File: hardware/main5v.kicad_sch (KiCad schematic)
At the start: 4 parts, among them U701 TPS56837RPAR

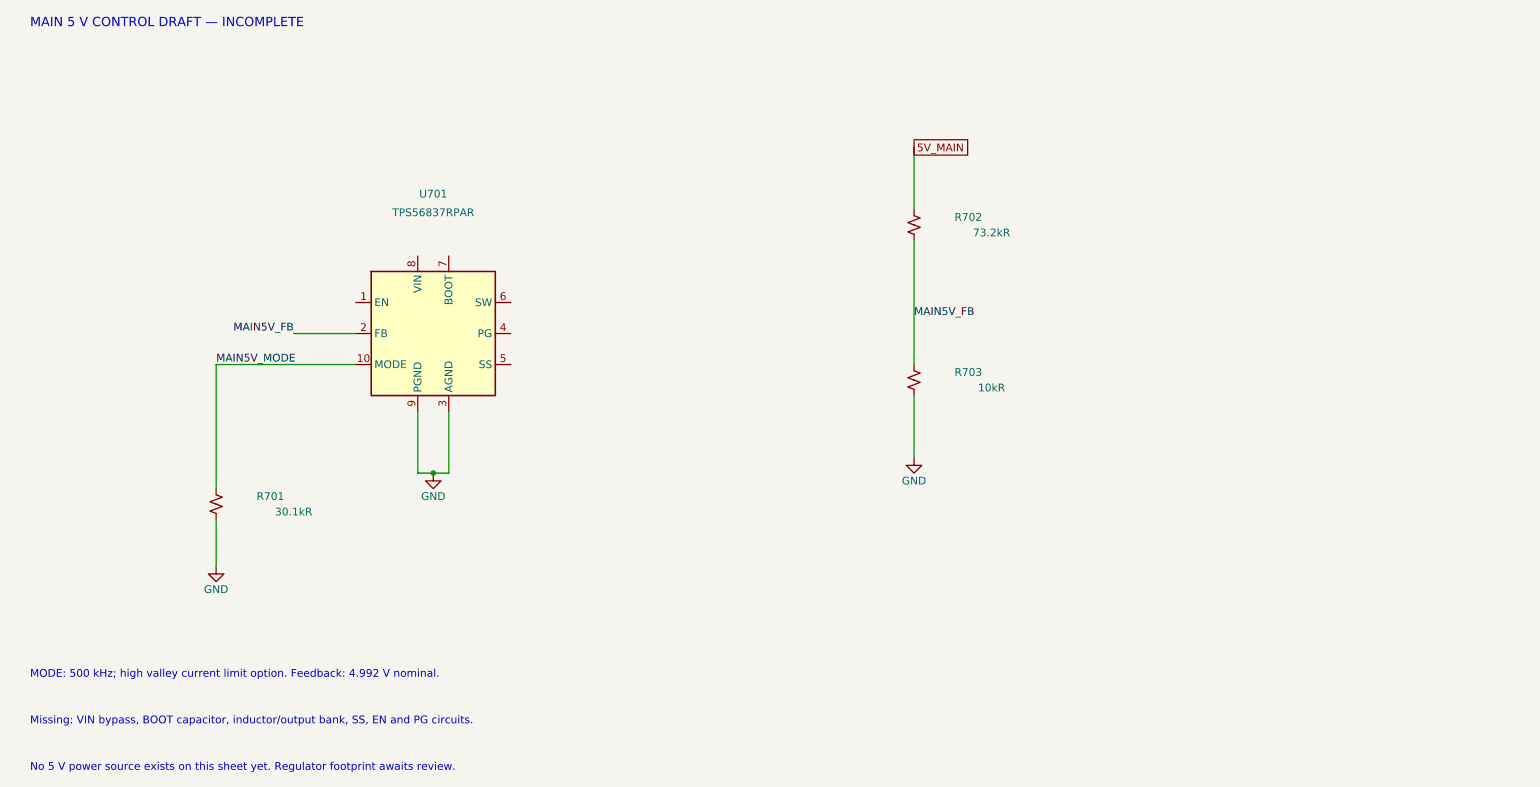
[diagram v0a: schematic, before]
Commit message: Capture main 5 V bootstrap capacitor with native connectivity checks
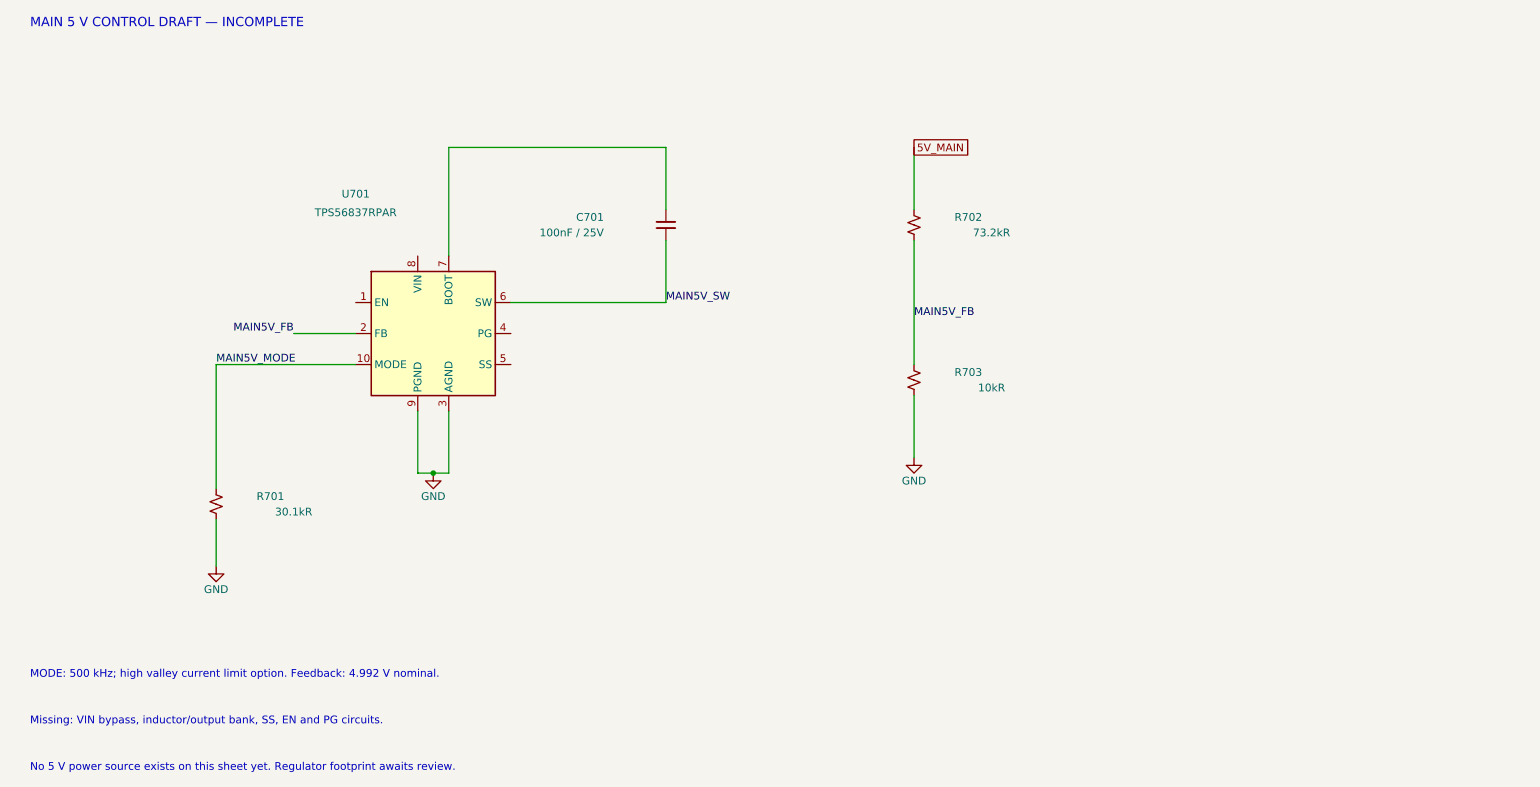
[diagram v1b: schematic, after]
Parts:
- added C701: 100nF / 25V, Capacitor_SMD:C_0603_1608Metric, symbol Device:C_Small
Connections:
- net MAIN5V_SW: now reaches U701.6 (SW)
- net MAIN5V_SW: now also C701.2
- net at U701.7 (BOOT): now also C701.1
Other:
- note added: "Missing: VIN bypass, inductor/output bank, SS, EN and PG circuits."
- note removed: "Missing: VIN bypass, BOOT capacitor, inductor/output bank, SS, EN and PG circuits."

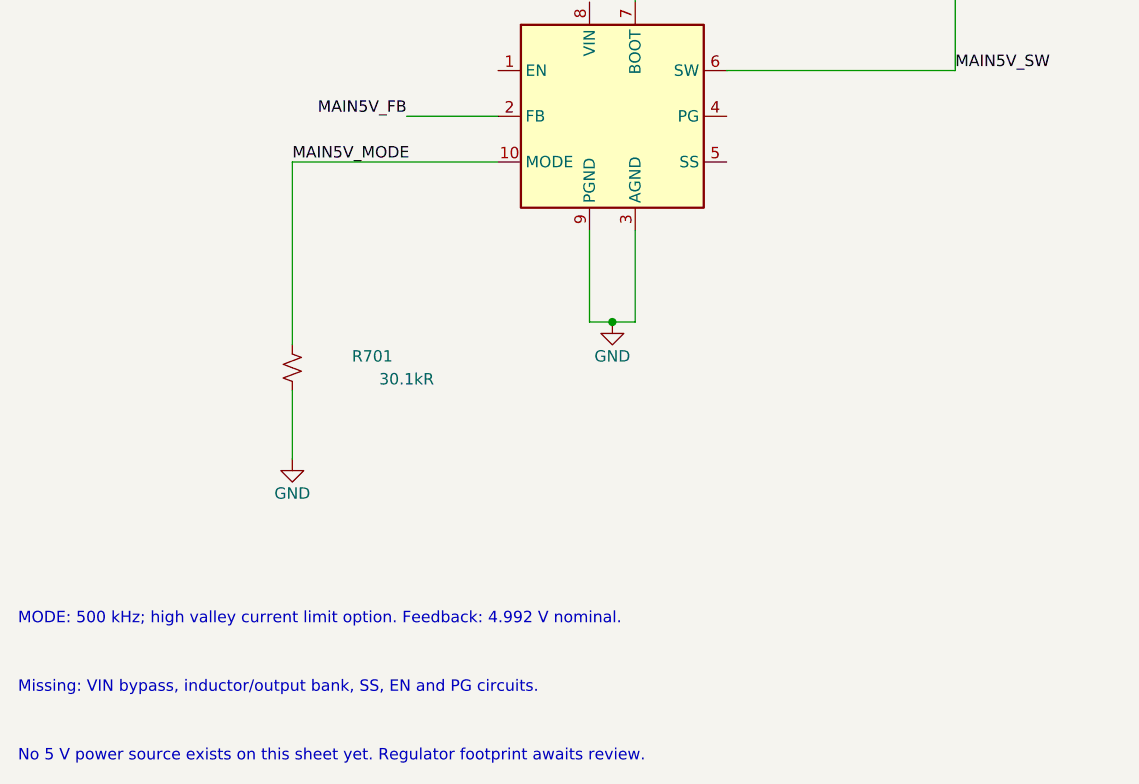
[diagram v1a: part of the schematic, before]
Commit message: Capture main 5 V soft start with exact manufacturer capacitor
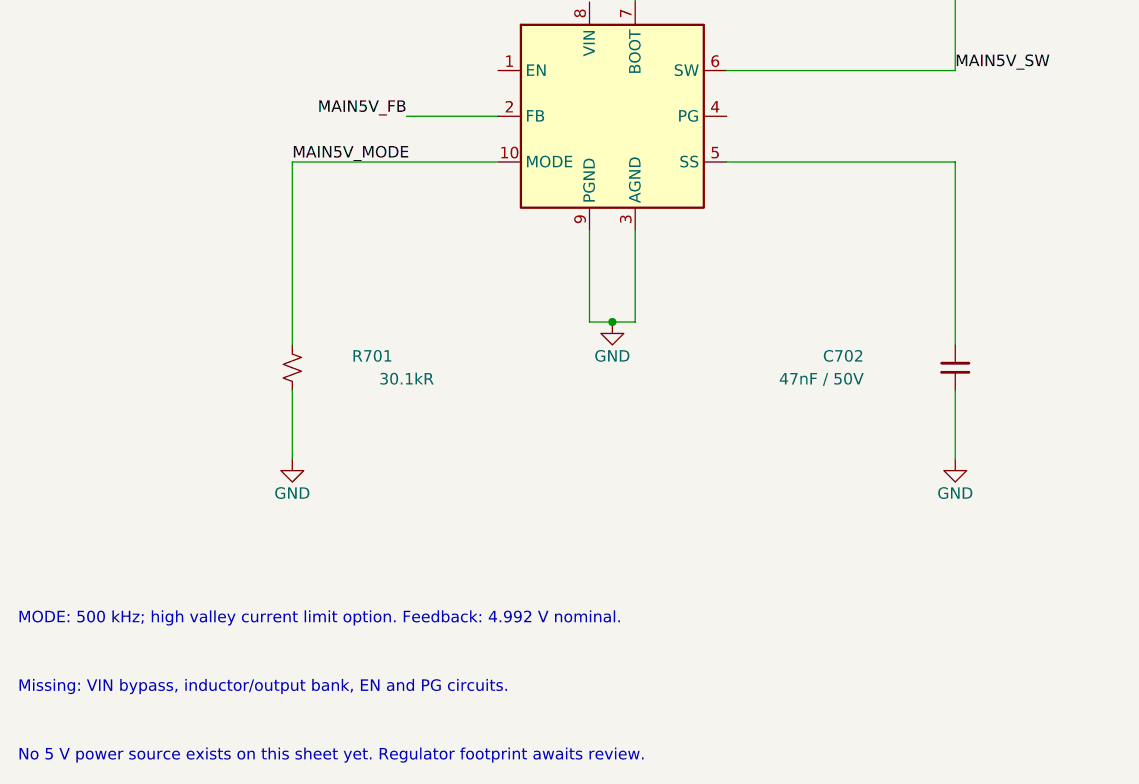
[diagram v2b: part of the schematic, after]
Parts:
- added C702: 47nF / 50V, Capacitor_SMD:C_0603_1608Metric, symbol Device:C_Small
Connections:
- net GND: now also C702.2
- net at U701.5 (SS): now also C702.1
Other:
- note added: "Missing: VIN bypass, inductor/output bank, EN and PG circuits."
- note removed: "Missing: VIN bypass, inductor/output bank, SS, EN and PG circuits."

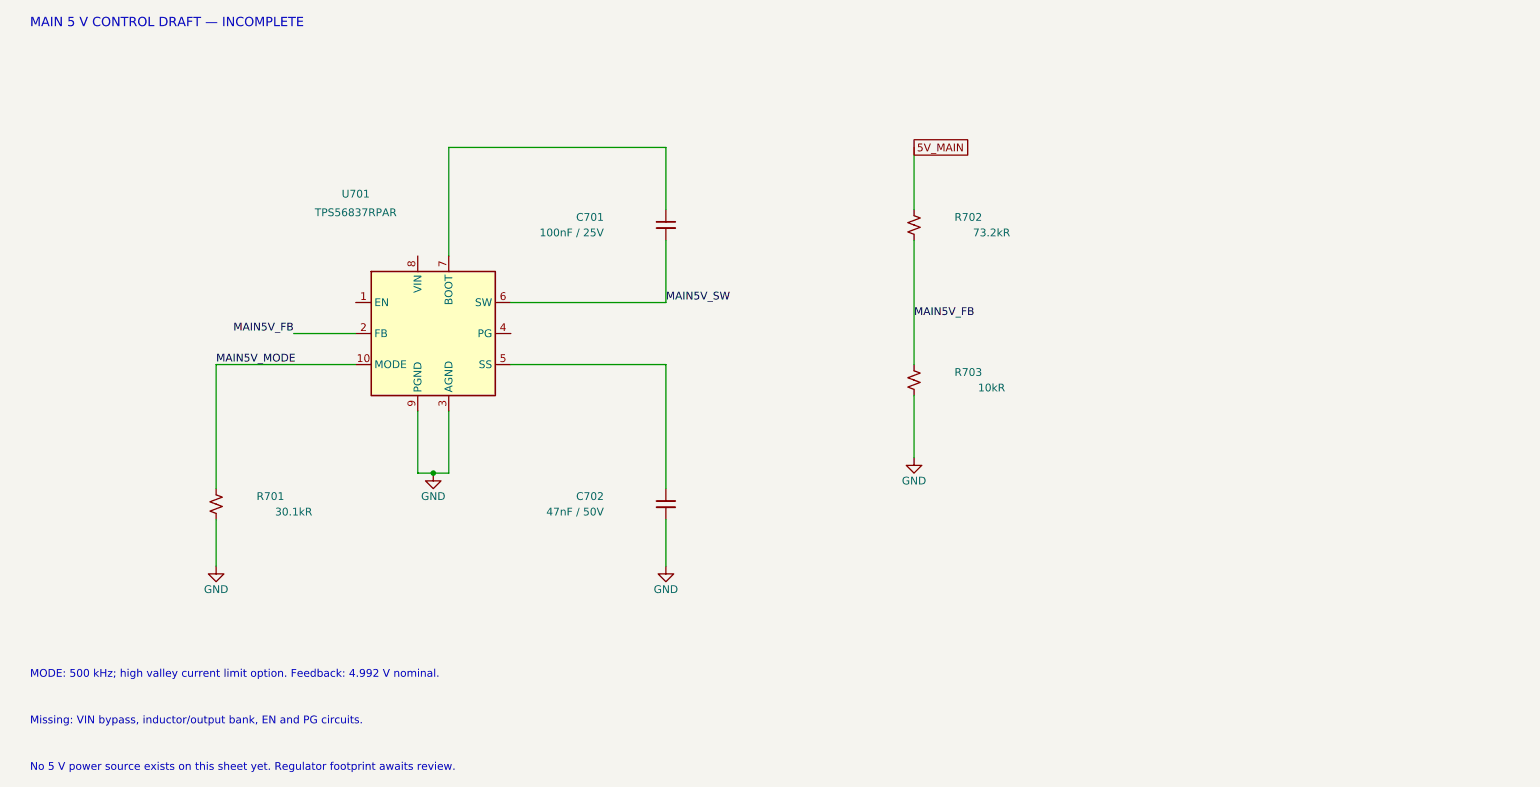
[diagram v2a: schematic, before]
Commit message: Capture main 5 V input bypass and join isolated 12 V rail
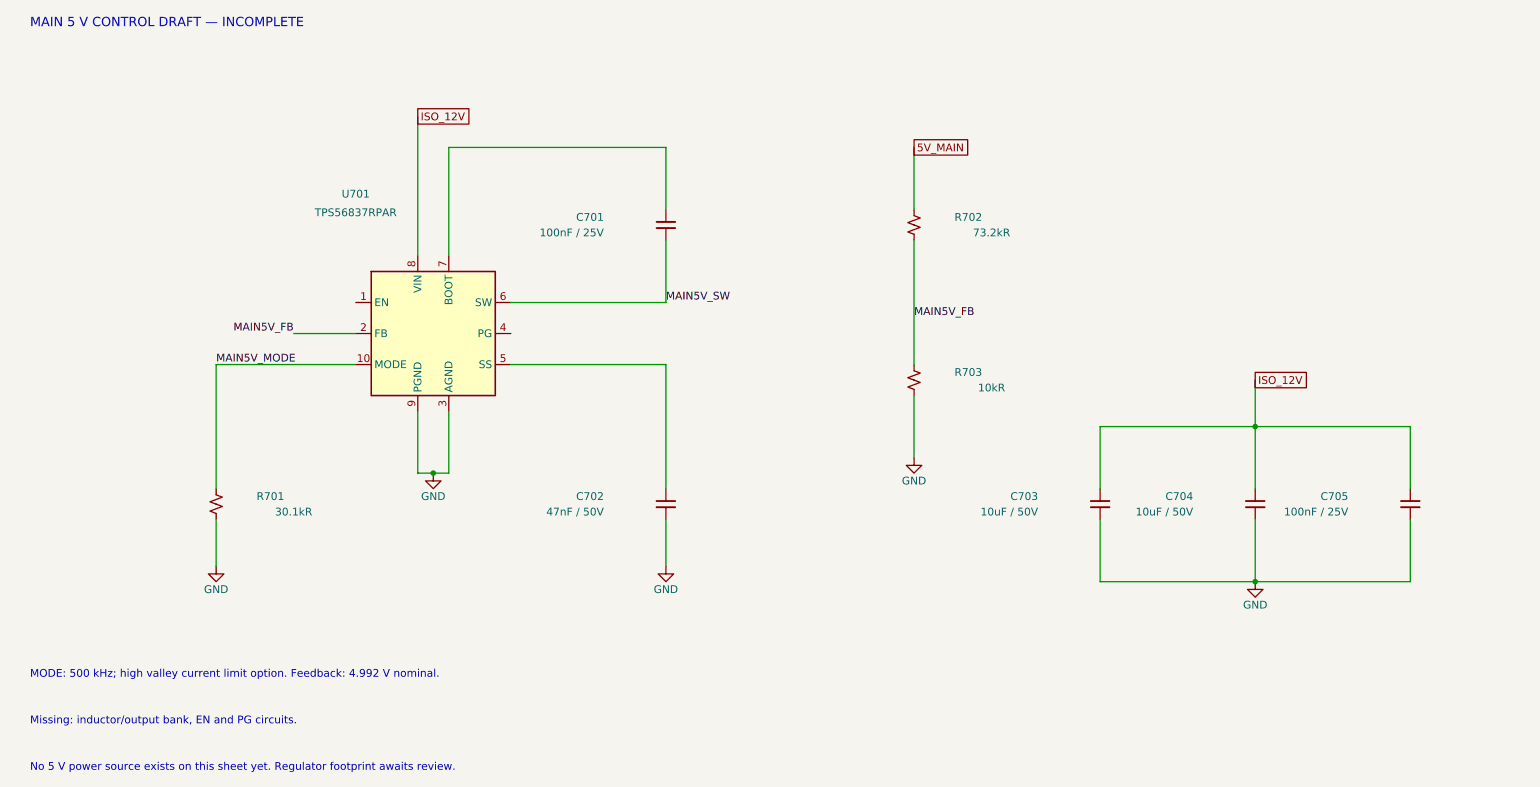
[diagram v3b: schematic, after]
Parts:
- added C703, C704: 10uF / 50V, Capacitor_SMD:C_1206_3216Metric, symbol Device:C_Small
- added C705: 100nF / 25V, Capacitor_SMD:C_0603_1608Metric, symbol Device:C_Small
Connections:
- net GND: now also C703.2, C704.2, C705.2
- net ISO_12V: now reaches U701.8 (VIN)
- net ISO_12V: now also C703.1, C704.1, C705.1
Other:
- note added: "Missing: inductor/output bank, EN and PG circuits."
- note removed: "Missing: VIN bypass, inductor/output bank, EN and PG circuits."

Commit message: Connect recovery MCU to main 5 V enable with external pulldown
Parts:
- added R704: 1kR, Resistor_SMD:R_0603_1608Metric, symbol Device:R_Small_US
- added R705: 10kR, Resistor_SMD:R_0603_1608Metric, symbol Device:R_Small_US
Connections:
- net GND: now also R705.2
- net at U701.1 (EN): now also R704.2, R705.1
- new net MCU_MAIN5V_EN: R704.1
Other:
- note added: "Missing: inductor/output bank and PG circuits."
- note removed: "Missing: inductor/output bank, EN and PG circuits."

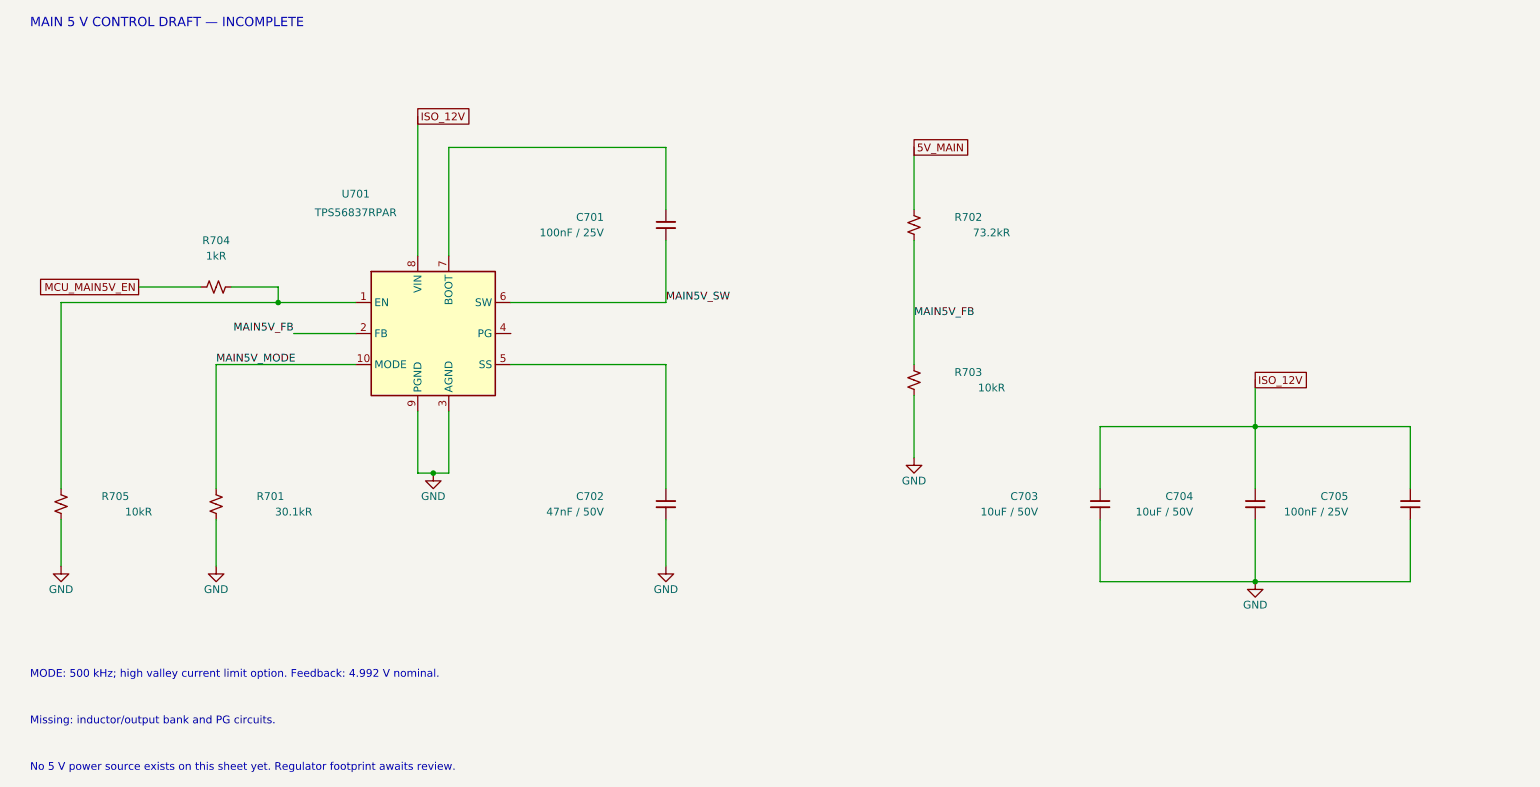
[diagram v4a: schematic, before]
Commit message: Connect main 5 V power good to recovery-domain MCU input
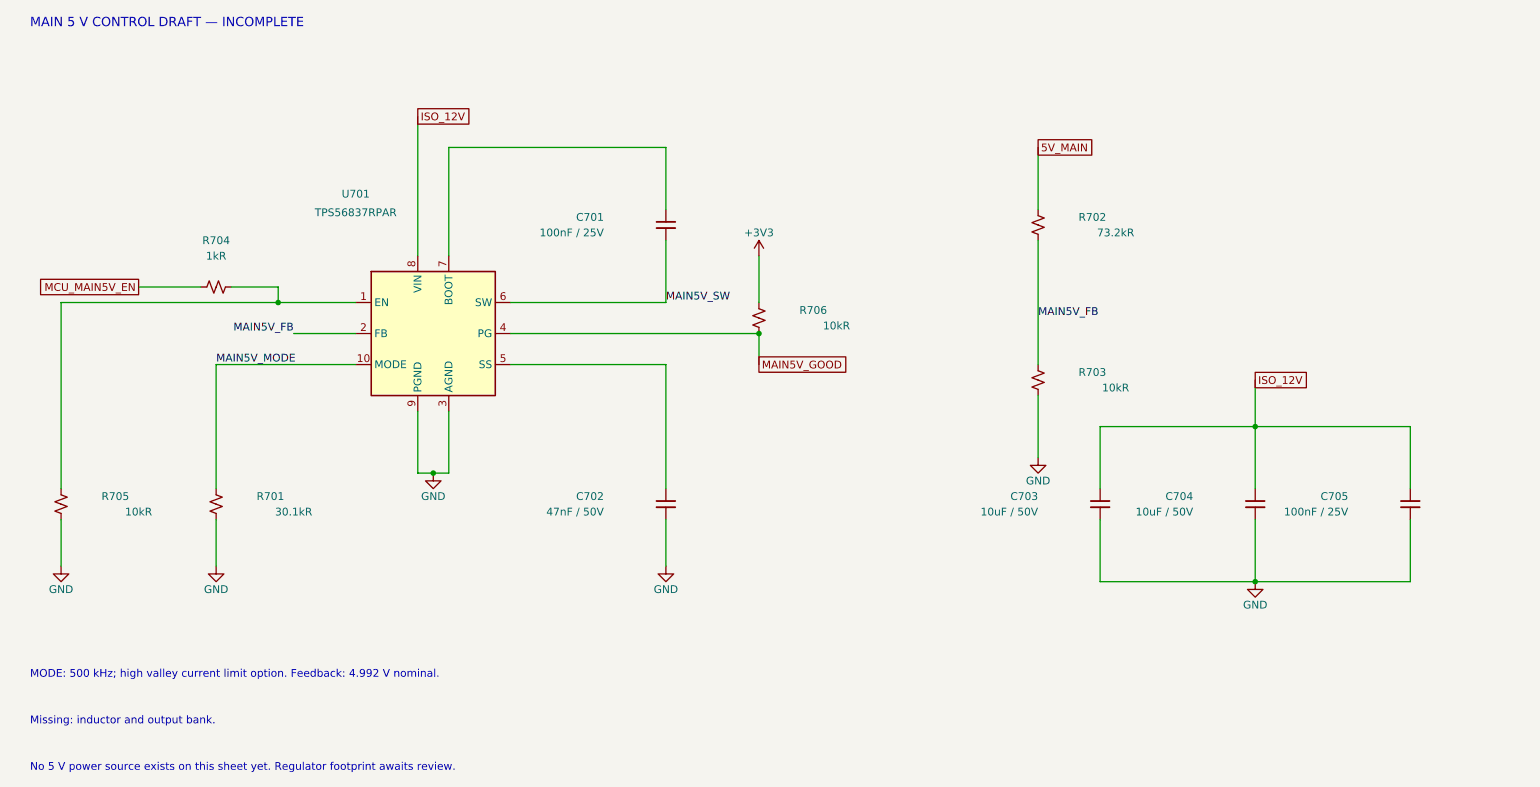
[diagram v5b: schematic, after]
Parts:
- added R706: 10kR, Resistor_SMD:R_0603_1608Metric, symbol Device:R_Small_US
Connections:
- net MAIN5V_GOOD: now reaches U701.4 (PG)
- net MAIN5V_GOOD: now also R706.2
- new net +3V3: R706.1
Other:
- note added: "Missing: inductor and output bank."
- note removed: "Missing: inductor/output bank and PG circuits."
- moved on the sheet: R702, R703
